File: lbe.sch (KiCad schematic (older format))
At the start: 16 parts, among them J1 Screw_Terminal_1x03, M1 BLUEPILL_STM8S103F3, U1 SN74LV1T34

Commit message: Layout complete
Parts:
- added C10: 100n, Capacitors_SMD:C_0603_HandSoldering, symbol C_Small
- added J10: Screw_Terminal_1x02, Connectors_Phoenix:PhoenixContact_MC-G_02x3.81mm_Angled, symbol Screw_Terminal_1x02
- C5: footprint Capacitors_SMD:C_0603_HandSoldering -> footprints:Cap_electrolytic_8x10
- M1: footprint Pin_Headers:Pin_Header_Straight_2x10_Pitch2.54mm -> footprints:BLUEPILL_STM8S103F3
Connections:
- wire segments 83 -> 93
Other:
- moved on the sheet: C1, C2, C3

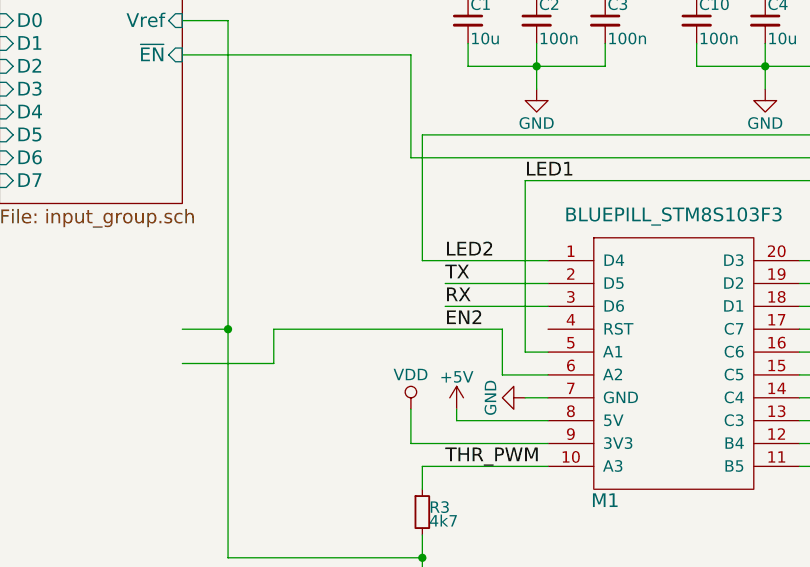
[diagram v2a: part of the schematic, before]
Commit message: Add serial header, restore holes
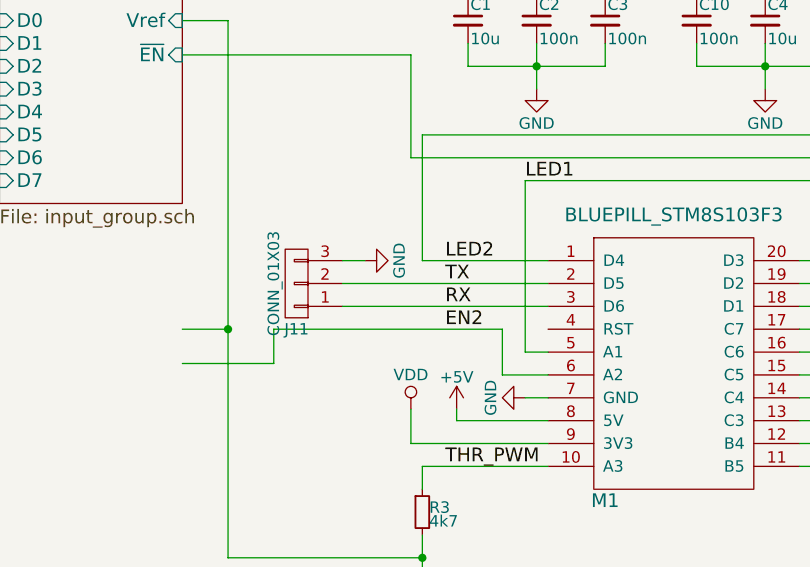
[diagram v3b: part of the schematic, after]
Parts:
- added J11: CONN_01X03, Pin_Headers:Pin_Header_Straight_1x03_Pitch2.54mm, symbol CONN_01X03
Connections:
- wire segments 93 -> 94
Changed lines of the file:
@@
 	6250 3200 7700 3200
 Wire Wire Line
-	4700 3400 5150 3400
-Wire Wire Line
-	4700 3300 5150 3300
+	4250 3400 5150 3400
+Wire Wire Line
+	4250 3300 5150 3300
 Wire Wire Line
 	2550 4200 2750 4200
@@
 	4950 3700 4950 3500
 Wire Wire Line
+	3950 3500 3950 3650
+Wire Wire Line
+	3950 3650 3550 3650
+Wire Wire Line
+	4550 2300 4550 2750
+Wire Wire Line
+	4550 2750 6900 2750
+Wire Wire Line
+	6900 2750 6900 4100
+Wire Wire Line
+	6900 4100 6250 4100
+Wire Wire Line
+	5150 3200 4600 3200
+Wire Wire Line
+	4600 3200 4600 2650
+Wire Wire Line
+	4600 2650 7350 2650
+Wire Wire Line
+	7350 2650 7350 2600
+Wire Wire Line
+	9300 2400 9300 2300
+Wire Wire Line
+	9300 2300 9400 2300
+Wire Wire Line
+	9400 2100 9300 2100
+Wire Wire Line
+	9300 2100 9300 2000
+Wire Wire Line
+	5800 2350 5800 2250
+Wire Wire Line
+	5800 2050 5800 1950
+$Comp
+L CONN_01X03 J11
+U 1 1 5AD75C61
+P 4050 3300
+F 0 "J11" H 4050 3500 50  0000 C CNN
+F 1 "CONN_01X03" V 4150 3300 50  0000 C CNN
+F 2 "Pin_Headers:Pin_Header_Straight_1x03_Pitch2.54mm" H 4050 3300 50  0001 C CNN
+F 3 "" H 4050 3300 50  0001 C CNN
+	1    4050 3300
+	-1   0    0    1
+$EndComp
+$Comp
+L GND #PWR017
+U 1 1 5AD75F9A
+P 4350 3200
+F 0 "#PWR017" H 4350 2950 50  0001 C CNN
+F 1 "GND" H 4350 3050 50  0000 C CNN
+F 2 "" H 4350 3200 50  0001 C CNN
+F 3 "" H 4350 3200 50  0001 C CNN
+	1    4350 3200
+	0    -1   -1   0
+$EndComp
+Wire Wire Line
+	4350 3200 4250 3200
+Wire Wire Line
 	4950 3500 3950 3500
-Wire Wire Line
-	3950 3500 3950 3650
-Wire Wire Line
-	3950 3650 3550 3650
-Wire Wire Line
-	4550 2300 4550 2750
-Wire Wire Line
-	4550 2750 6900 2750
-Wire Wire Line
-	6900 2750 6900 4100
-Wire Wire Line
-	6900 4100 6250 4100
-Wire Wire Line
-	5150 3200 4600 3200
-Wire Wire Line
-	4600 3200 4600 2650
-Wire Wire Line
-	4600 2650 7350 2650
-Wire Wire Line
-	7350 2650 7350 2600
-Wire Wire Line
-	9300 2400 9300 2300
-Wire Wire Line
-	9300 2300 9400 2300
-Wire Wire Line
-	9400 2100 9300 2100
-Wire Wire Line
-	9300 2100 9300 2000
-Wire Wire Line
-	5800 2350 5800 2250
-Wire Wire Line
-	5800 2050 5800 1950
 $EndSCHEMATC
